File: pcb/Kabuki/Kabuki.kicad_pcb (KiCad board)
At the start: 2 copper layers, 70 x 40 mm, 14 parts, among them J1 NC3FAHL1, J2 NC3MAHR, J3 Solenoide, Q1 FQD18N20V2TM, Q2 FQD18N20V2TM, U1 IX4428N

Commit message: update
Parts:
- added C4: capcer0805, Kabuki:CAP0805, F.Cu at (129.6, 69.0)
- C2, C3, J1, J2: moved to B.Cu
- moved R1 19.8 mm to (147.0, 75.5)
- moved Q1 16.6 mm to (144.5, 82.0), turned to 270 degrees
- moved D3 16.5 mm to (119.5, 75.0)
- moved J3 16.5 mm to (121.5, 81.0)
- moved Q2 14.2 mm to (130.0, 82.0), turned to 270 degrees
- moved R2 12.3 mm to (129.6, 66.5), turned to 180 degrees
- moved C1 6.67 mm to (139.5, 71.5)
- moved C2 3.20 mm to (107.5, 82.0), turned to 90 degrees
- moved C3 3.20 mm to (162.5, 82.0), turned to 90 degrees
- moved D1 2.83 mm to (120.0, 58.0), turned to 270 degrees
- moved J2 2.83 mm to (97.0, 58.0), turned to 270 degrees
- moved J1 2.26 mm to (173.0, 58.0), turned to 90 degrees
- moved D2 2.24 mm to (150.0, 58.0), turned to 90 degrees
- moved U1 2.12 mm to (135.5, 71.5)
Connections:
- U1 pad 5: Net-(Q1-Pad1) -> Net-(Q2-Pad1)
- U1 pad 7: Net-(Q2-Pad1) -> Net-(Q1-Pad1)
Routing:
- net GND: track 160.9 -> 219.4 mm
- net +5VD: track 103.5 -> 75.2 mm
- net Net-(D1-Pad3): track 45.1 -> 66.3 mm
- net Net-(C2-Pad1): track 71.0 -> 64.1 mm
- net Net-(Q1-Pad3): track 11.6 -> 5.56 mm
- net Net-(D3-PadC): track 10.2 -> 13.7 mm
- net Net-(C4-Pad2): track 10.7 -> 13.0 mm
- net Net-(Q1-Pad1): track 7.56 -> 9.03 mm
- net Net-(Q2-Pad1): track 11.5 -> 12.2 mm
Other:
- board size 70 x 40 mm -> 70 x 42 mm
- board text added: "tapbuki driver v1.0 2020-02-01"

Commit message: update
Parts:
- added G***: LOGO, Kabuki:tapbuki, F.Cu at (134.0, 58.0)
- added R3: 1k, Kabuki:RES0805, F.Cu at (129.6, 71.0)
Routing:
- net GND: track 219.4 -> 222.1 mm
- net Net-(C4-Pad2): track 13.0 -> 15.0 mm

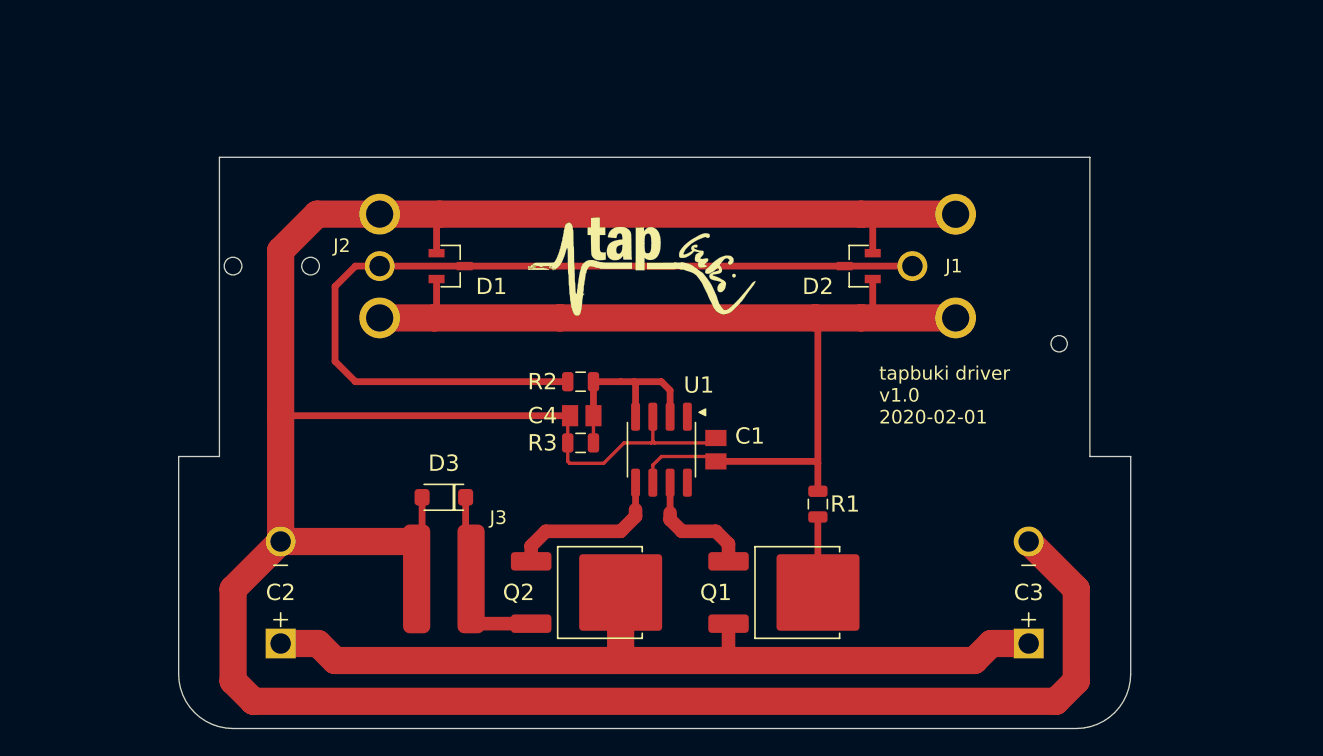
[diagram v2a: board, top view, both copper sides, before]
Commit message: add sim add PMOS
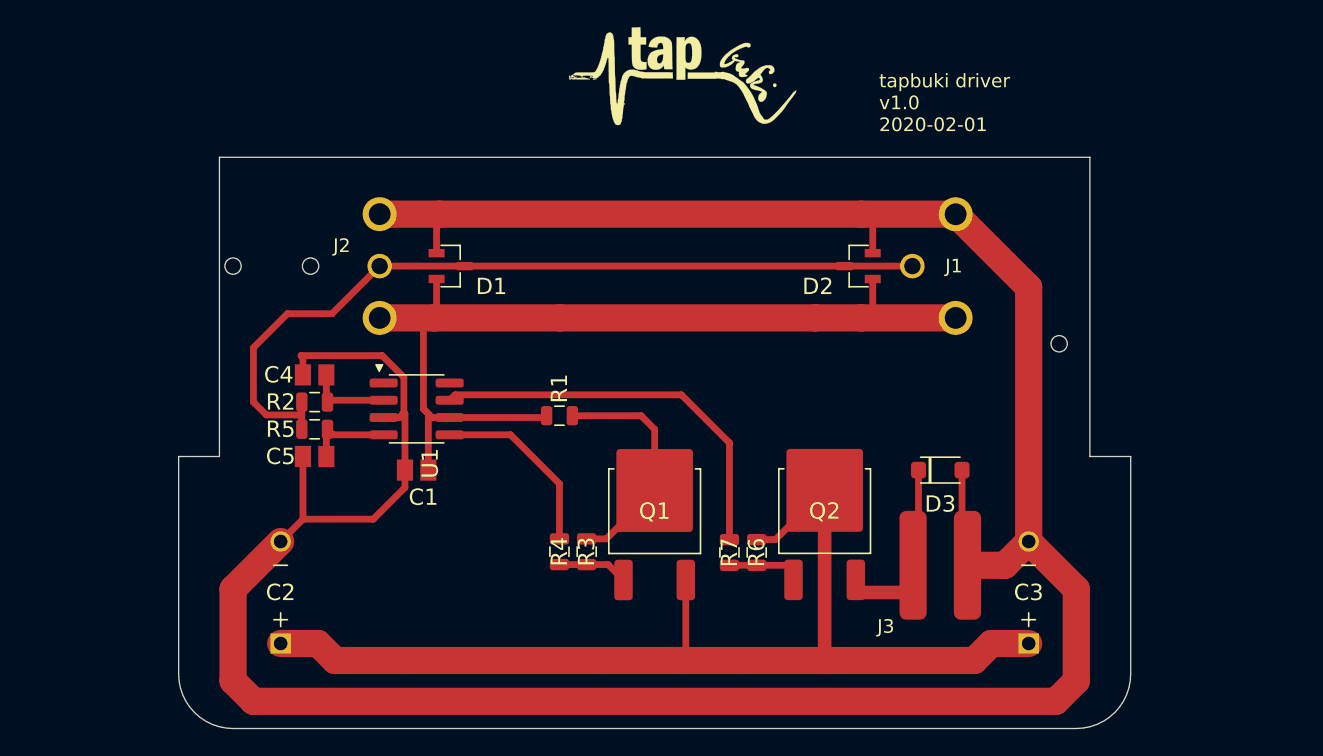
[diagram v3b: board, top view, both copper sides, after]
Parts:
- added C5: capcer0805, Kabuki:CAP0805, F.Cu at (110.0, 72.0)
- added R4: 220, Kabuki:RES0805, F.Cu at (128.0, 79.0)
- added R5: 1k, Kabuki:RES0805, F.Cu at (110.0, 70.0)
- added R6: 220, Kabuki:RES0805, F.Cu at (142.5, 79.1)
- added R7: 220, Kabuki:RES0805, F.Cu at (140.5, 79.1)
- Q1, Q2: value FQD18N20V2TM -> FQD17P06
- R3: value 1k -> 220
- moved D3 36.6 mm to (156.0, 73.0), turned to 0 degrees
- moved J3 32.5 mm to (154.0, 80.0), turned to 0 degrees
- moved C1 22.1 mm to (117.5, 73.0), turned to 180 degrees
- moved R1 20.1 mm to (128.0, 69.0), turned to 0 degrees
- moved C4 19.9 mm to (110.0, 66.0)
- moved R2 19.6 mm to (110.0, 68.0)
- moved U1 18.2 mm to (117.5, 68.5), turned to 270 degrees
- moved Q2 18.2 mm to (147.5, 77.0), turned to 0 degrees
- moved G*** 14.3 mm to (137.0, 44.0)
- moved Q1 10.7 mm to (135.0, 77.0), turned to 0 degrees
- moved R3 8.01 mm to (130.0, 79.0), turned to 270 degrees
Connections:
- R3 pad 1: Net-(C4-Pad2) -> Net-(Q1-Pad3)
- R3 pad 2: GND -> Net-(Q1-Pad1)
- U1 pad 4: Net-(C4-Pad2) -> Net-(C5-Pad2)
- U1 pad 5: Net-(Q2-Pad1) -> Net-(R4-Pad1)
- U1 pad 7: Net-(Q1-Pad1) -> Net-(R7-Pad2)
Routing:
- net Net-(R7-Pad2): track 0.00 -> 29.3 mm
- net Net-(C2-Pad1): track 64.1 -> 79.1 mm
- net Net-(R4-Pad1): track 0.00 -> 13.6 mm
- net GND: track 222.1 -> 208.7 mm
- net Net-(Q1-Pad3): track 5.56 -> 17.4 mm
- net Net-(C4-Pad2): track 15.0 -> 6.22 mm
- net Net-(C5-Pad2): track 0.00 -> 6.33 mm
- net Net-(Q2-Pad1): track 12.2 -> 6.28 mm
- net +5VD: track 75.2 -> 69.5 mm
- net Net-(D1-Pad3): track 66.3 -> 60.9 mm
- net Net-(Q1-Pad1): track 9.03 -> 5.18 mm
- net Net-(D3-PadC): track 13.7 -> 14.9 mm

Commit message: update
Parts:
- moved G*** 14.0 mm to (135.9, 58.0)
- moved D3 5.12 mm to (153.5, 68.6)
- moved J3 5.12 mm to (151.5, 75.6)
- moved Q1 4.53 mm to (130.5, 77.5)
- moved Q2 4.53 mm to (143.0, 77.5)
- moved R3 4.53 mm to (125.5, 79.5)
- moved R4 4.53 mm to (123.5, 79.5)
- moved R6 4.53 mm to (138.0, 79.6)
- moved R7 4.53 mm to (136.0, 79.6)
- moved R1 2.50 mm to (130.5, 69.1), turned to 270 degrees
- moved C1 1.50 mm to (117.5, 71.5)
- moved U1 1.00 mm to (117.5, 67.5)
- moved C4 0.89 mm to (110.0, 65.1)
- moved C5 0.89 mm to (110.0, 71.1)
- moved R2 0.89 mm to (110.0, 67.1)
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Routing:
- net Net-(D3-PadC): track 14.9 -> 21.2 mm
- net Net-(Q1-Pad3): track 17.4 -> 11.4 mm
- net Net-(D1-Pad3): track 60.9 -> 56.0 mm
- net GND: track 208.7 -> 213.4 mm
- net Net-(R7-Pad2): track 29.3 -> 26.6 mm
- net Net-(R4-Pad1): track 13.6 -> 11.8 mm
- net +5VD: track 69.5 -> 70.7 mm
- net Net-(C2-Pad1): track 79.1 -> 78.2 mm
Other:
- board size 70 x 42 mm -> 64 x 40 mm
- board text added: "tapbuki driver v1.0 Feb. 2020"
- board text removed: "tapbuki driver v1.0 2020-02-01"

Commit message: update and order
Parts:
- added R8: 10k, Kabuki:RES0805, F.Cu at (158.5, 82.0)
- added R9: 10k, Kabuki:RES0805, F.Cu at (110.0, 62.5)
- Q1: footprint Kabuki:DPAK4P229_FQD18N20V2 -> Kabuki:DPAK4P229_FQD17P06
- Q2: value FQD17P06 -> FQD18N20V2TM
- R3, R6: value 220 -> 1k
- R4, R7: value 220 -> 470
- moved R6 19.8 mm to (155.0, 69.5), turned to 180 degrees
- moved R7 18.5 mm to (151.5, 69.5), turned to 180 degrees
- moved D3 14.1 mm to (139.5, 70.6)
- moved J3 14.1 mm to (137.5, 77.6)
- moved R1 12.9 mm to (131.0, 82.0)
- moved R4 10.0 mm to (124.5, 69.5), turned to 0 degrees
- moved R3 8.06 mm to (124.5, 71.5), turned to 0 degrees
- moved Q2 8.03 mm to (151.0, 76.5), turned to 90 degrees
- moved Q1 2.25 mm to (128.5, 76.5), turned to 270 degrees
- moved G*** 0.09 mm to (136.0, 58.0)
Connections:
- D3 pad A: GND -> Net-(D3-PadA)
- D3 pad C: Net-(D3-PadC) -> Net-(C2-Pad1)
- J3 pad 1: Net-(D3-PadC) -> Net-(C2-Pad1)
- J3 pad 2: GND -> Net-(D3-PadA)
- Q1 pad 3: Net-(Q1-Pad3) -> +5VD
- Q2 pad 2: Net-(D3-PadC) -> GND
- Q2 pad 3: Net-(C2-Pad1) -> Net-(D3-PadA)
- R1 pad 1: +5VD -> Net-(Q1-Pad4)
- R1 pad 2: Net-(Q1-Pad3) -> Net-(C2-Pad1)
- R3 pad 1: Net-(Q1-Pad3) -> +5VD
- R6 pad 1: Net-(Q2-Pad1) -> GND
- R6 pad 2: Net-(C2-Pad1) -> Net-(Q2-Pad1)
- R7 pad 2: Net-(R7-Pad2) -> Net-(R4-Pad1)
- U1 pad 7: Net-(R7-Pad2) -> Net-(U1-Pad7)
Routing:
- net Net-(R7-Pad2): track 26.6 -> 0.00 mm
- net Net-(R4-Pad1): track 11.8 -> 35.5 mm
- net Net-(D3-PadC): track 21.2 -> 0.00 mm
- net Net-(D3-PadA): track 0.00 -> 14.6 mm
- net Net-(Q1-Pad3): track 11.4 -> 0.00 mm
- net GND: track 213.4 -> 220.7 mm
- net Net-(Q2-Pad1): track 6.28 -> 13.5 mm
- net +5VD: track 70.7 -> 76.0 mm
- net Net-(Q1-Pad4): track 0.00 -> 4.56 mm
- net Net-(C2-Pad1): track 78.2 -> 82.5 mm
- net Net-(D1-Pad3): track 56.0 -> 58.8 mm
